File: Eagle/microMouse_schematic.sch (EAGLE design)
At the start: 50 parts, among them IC1 DSPIC33FJ64MC804-PT, IC2 L293D, IC3 LM7805, IC4 LM7833, X1 22-23-2021

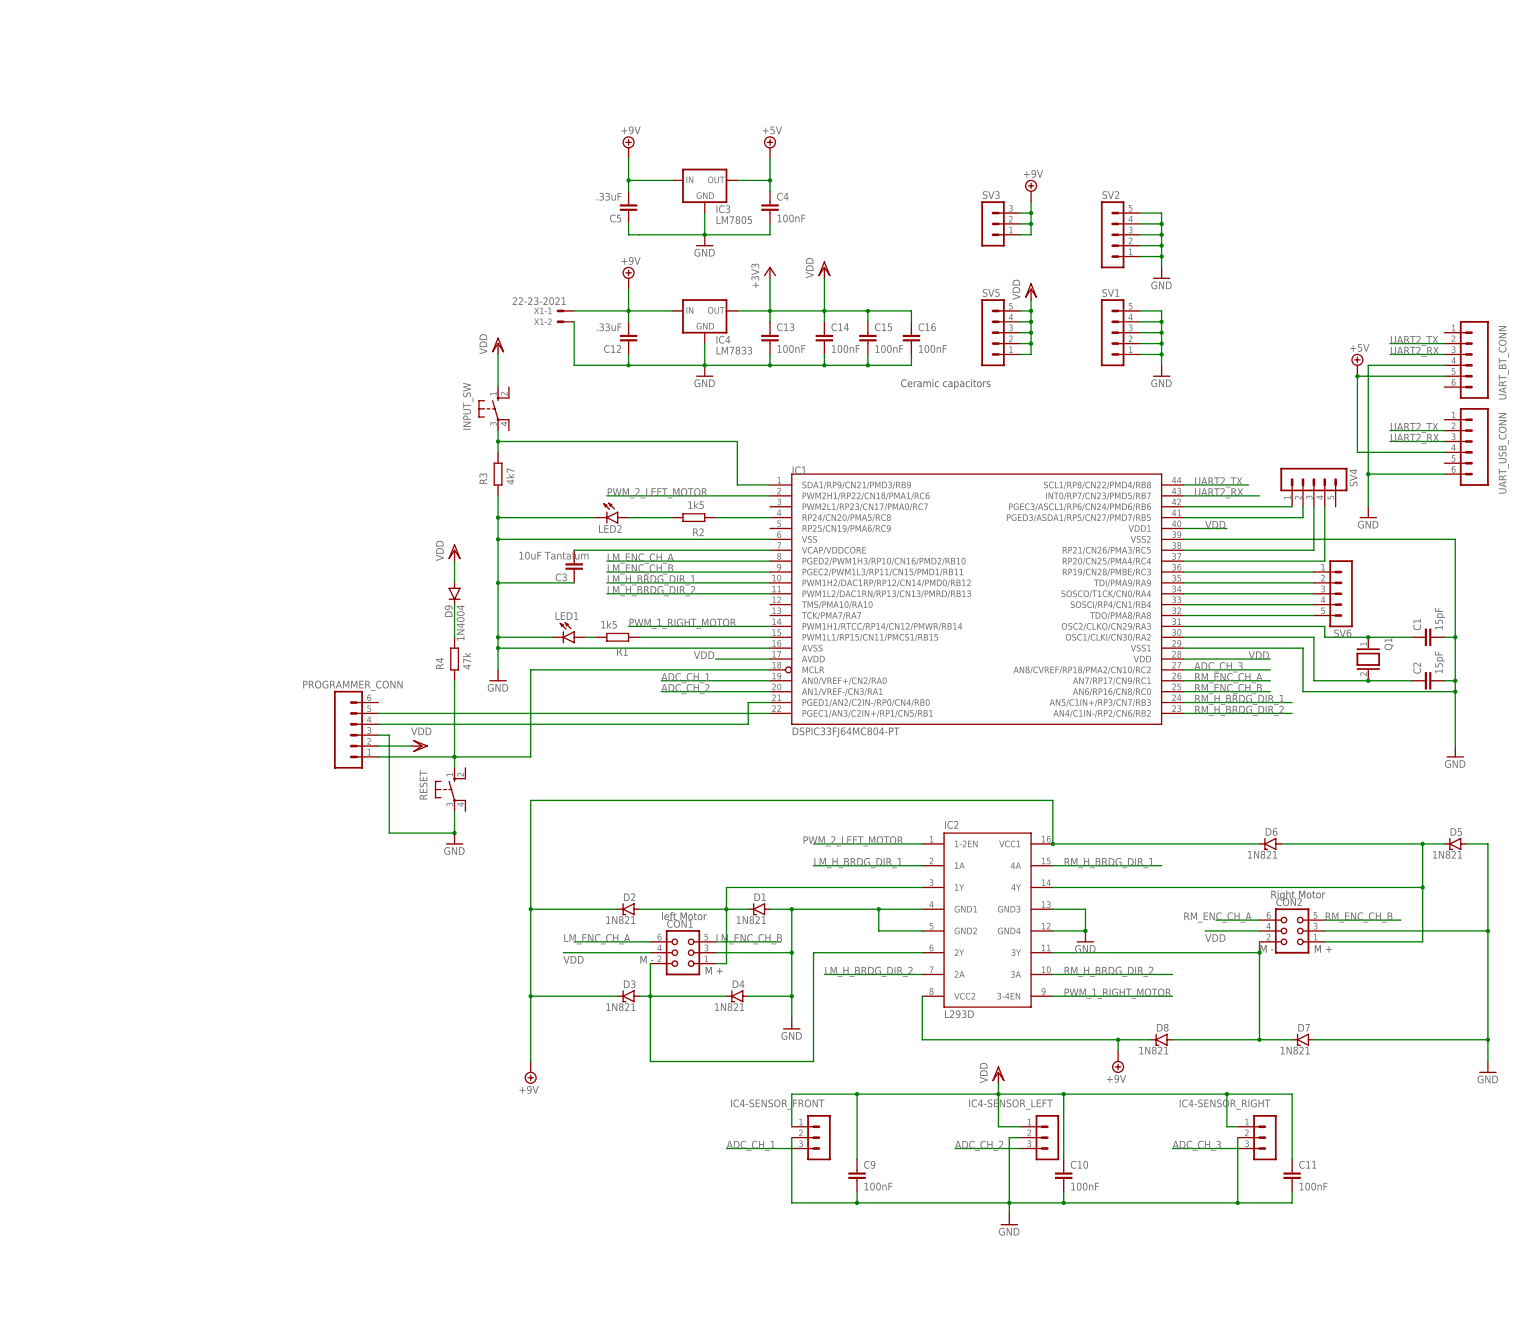
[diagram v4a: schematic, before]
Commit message: update schematic, finish placing components on board
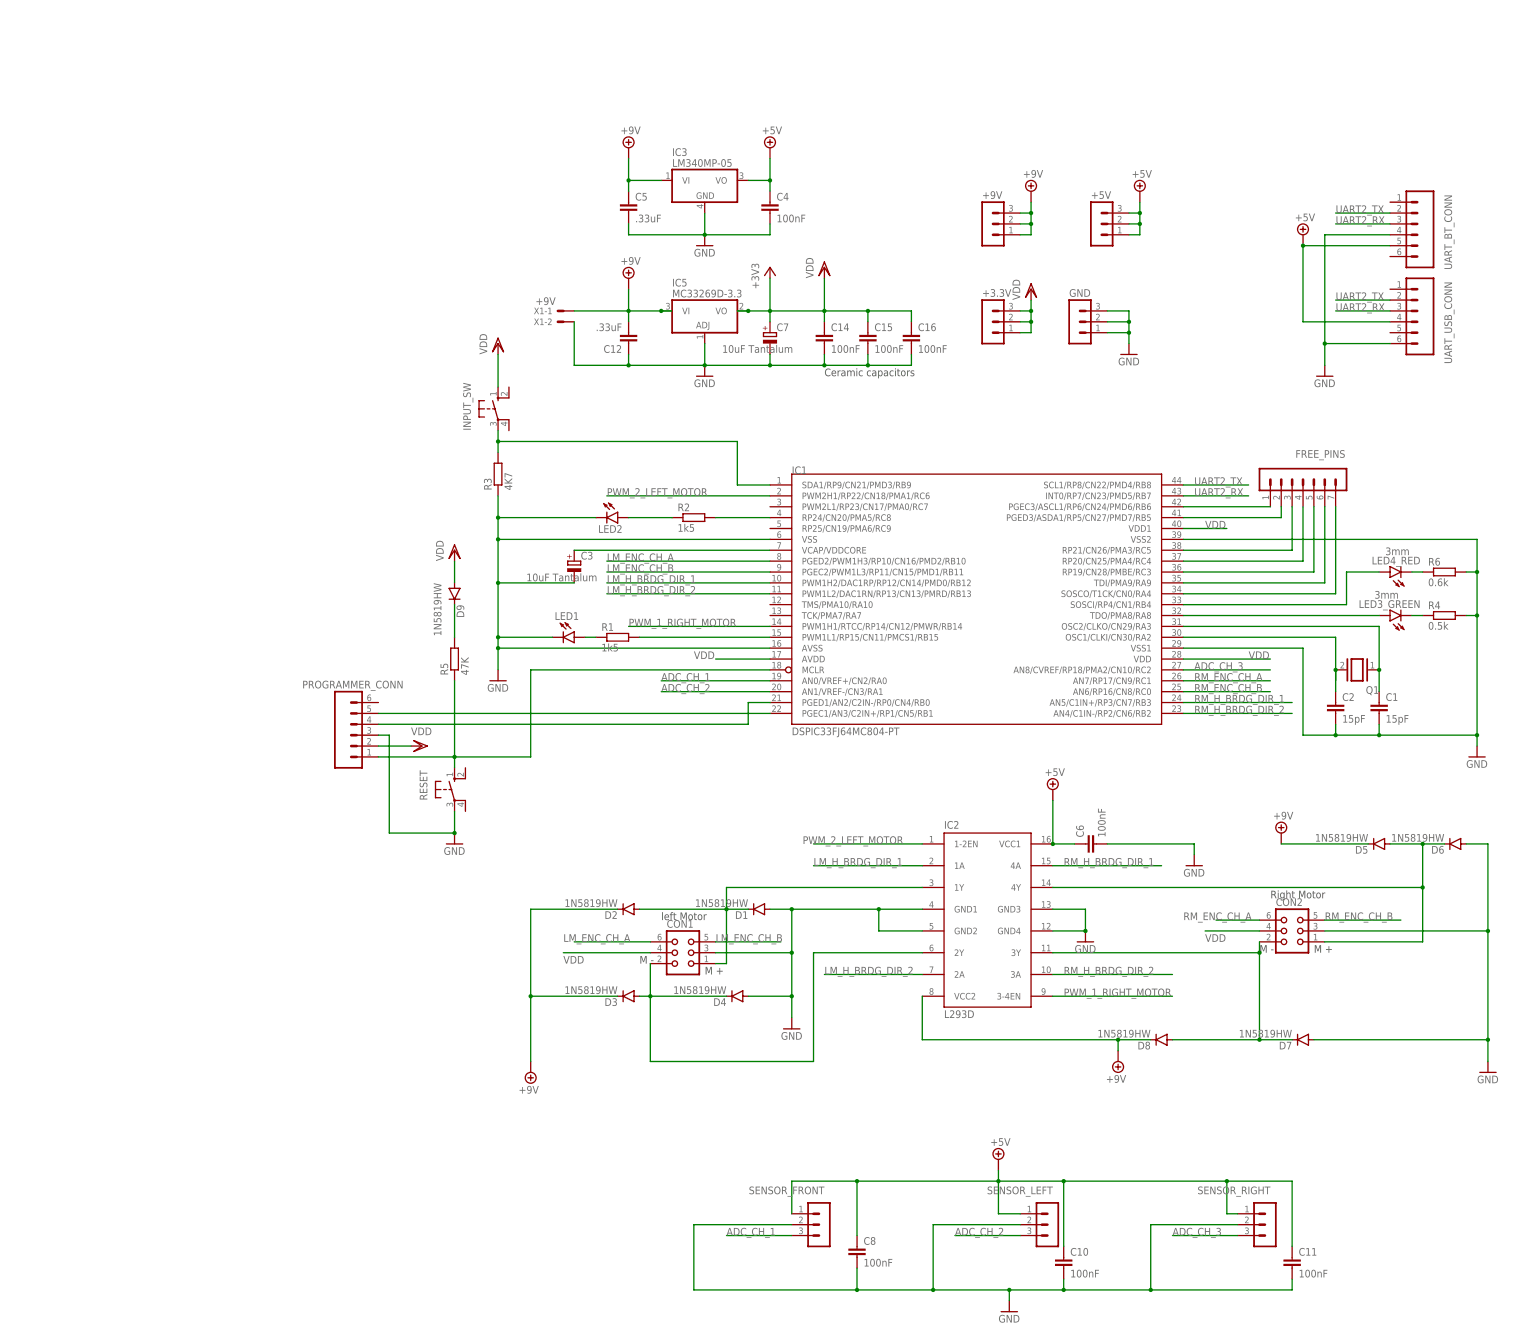
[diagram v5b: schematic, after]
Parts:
- removed C13, C9: 100nF, capacitor-wima:C2,5-3
- removed IC4: LM7833, v-reg:78XXS
- removed IC4-SENSOR_FRONT, IC4-SENSOR_LEFT, IC4-SENSOR_RIGHT: (no value), con-lstb:MA03-1
- removed SV1, SV2, SV4, SV5, SV6: (no value), con-lstb:MA05-1
- added +3.3V, +5V, GND, SENSOR_FRONT, SENSOR_LEFT, SENSOR_RIGHT: (no value), con-lstb:MA03-1
- added C6, C8: 100nF, rcl:C-EUC0805
- added C7: 10uF Tantalum, rcl:CPOL-EUCT3216
- added FREE_PINS: (no value), con-lstb:MA07-1
- added IC5: MC33269D-3.3, linear:MC33269D-3.3
- added LED3_GREEN, LED4_RED: 3mm, led:LEDB155
- added R5: 47K, rcl:R-EU_R0805
- added R6: 0.6k, rcl:R-EU_R0805
- C1, C10, C11, C12, C14, C15, C16, C2, C4, C5: device capacitor-wima:C2,5-3 -> rcl:C-EUC0805
- C3: device capacitor-wima:C2,5-3 -> rcl:CPOL-EUCT3216
- D1, D2, D3, D4, D5, D6, D7, D8: value 1N821 -> 1N5819HW; device diode:1N821 -> diode:CGRM4001-G
- D9: value 1N4004 -> 1N5819HW; device diode:1N4004 -> diode:CGRM4001-G
- IC3: value LM7805 -> LM340MP-05; device v-reg:78XXS -> linear:LM340MP-05
- R1, R2: device ngspice-simulation:R -> rcl:R-EU_R0805
- R3: value 4k7 -> 4K7; device ngspice-simulation:R -> rcl:R-EU_R0805
- R4: value 47k -> 0.5k; device ngspice-simulation:R -> rcl:R-EU_R0805
- X1: value 22-23-2021 -> +9V
- renumbered SV3 to +9V
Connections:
- new net N$13: LED3_GREEN.C, R4.1
- new net N$25: LED4_RED.C, R6.1
- net +5V: now also +5V.1, +5V.2, +5V.3, C10.1, C11.1, C6.1, C8.1, IC2.VCC1, IC3.VO, SENSOR_FRONT.1, SENSOR_LEFT.1, SENSOR_RIGHT.1; no longer IC3.OUT
- net +9V: now also C5.1, D5.C, IC3.VI, IC5.VI; no longer C5.2, D6.C, IC2.VCC1, IC3.IN, IC4.IN
- net ADC_CH_1: now also SENSOR_FRONT.3; no longer IC4-SENSOR_FRONT.3
- net ADC_CH_2: now also SENSOR_LEFT.3; no longer IC4-SENSOR_LEFT.3
- net ADC_CH_3: now also SENSOR_RIGHT.3; no longer IC4-SENSOR_RIGHT.3
- net GND: now also C3.-, C5.2, C6.2, C7.-, C8.2, D6.A, GND.1, GND.2, GND.3, IC5.ADJ, R4.2, R6.2, SENSOR_FRONT.2, SENSOR_LEFT.2, SENSOR_RIGHT.2; no longer C13.2, C3.1, C5.1, C9.2, D5.A, IC4-SENSOR_FRONT.2, IC4-SENSOR_LEFT.2, IC4-SENSOR_RIGHT.2, IC4.GND, SV1.1, SV1.2, SV1.3, SV1.4, SV1.5, SV2.1, SV2.2, SV2.3, SV2.4, SV2.5
- net N$1: now also R2.2; no longer R2.1
- net N$14: now also R1.2; no longer R1.1
- net N$15: now also LED4_RED.A; no longer SV6.4
- net N$16: now also FREE_PINS.7; no longer SV6.3
- net N$17: now also R1.1; no longer R1.2
- net N$18: now also FREE_PINS.6; no longer SV6.2
- net N$19: now also R5.2; no longer R4.2
- net N$2: now also D5.A, D6.C; no longer D5.C, D6.A
- net N$20: now also FREE_PINS.5; no longer SV6.1
- net N$21: now also FREE_PINS.4; no longer SV4.4
- net N$22: now also FREE_PINS.1; no longer SV4.1
- net N$23: now also FREE_PINS.2; no longer SV4.2
- net N$24: now also FREE_PINS.3; no longer SV4.3
- net N$3: now also R2.1; no longer R2.2
- net N$9: now also LED3_GREEN.A; no longer SV6.5
- net RESET: now also R5.1; no longer R4.1
- net VCAP/VDDCORE: now also C3.+; no longer C3.2
- net VDD: now also +3.3V.1, +3.3V.2, +3.3V.3, C7.+, IC5.VO; no longer C10.1, C11.1, C13.1, C9.1, IC4-SENSOR_FRONT.1, IC4-SENSOR_LEFT.1, IC4-SENSOR_RIGHT.1, IC4.OUT, SV5.1, SV5.2, SV5.3, SV5.4, SV5.5
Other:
- moved on the sheet: C1, C10, C11, C2, C5, Q1, R1, R2, R4, UART_BT_CONN, UART_USB_CONN

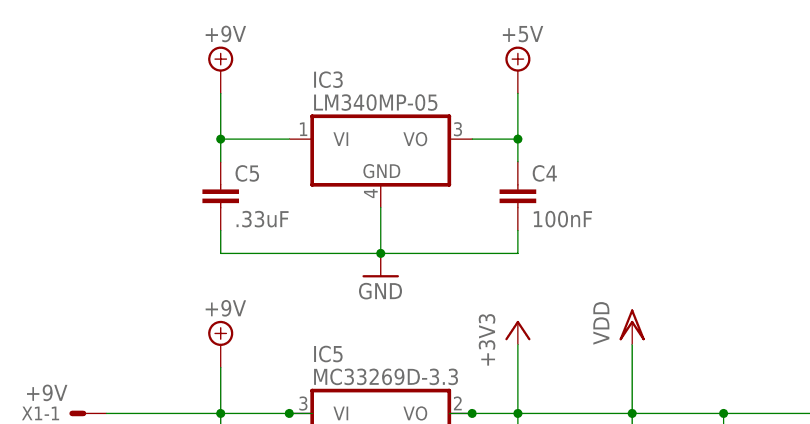
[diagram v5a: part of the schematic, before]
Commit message: PCB signals routing
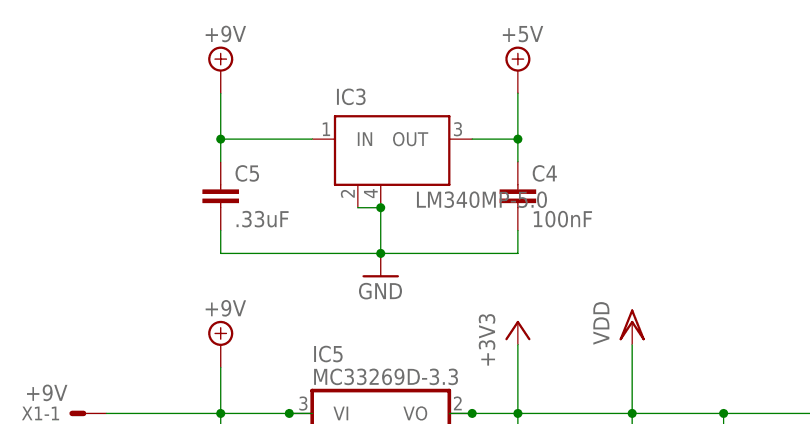
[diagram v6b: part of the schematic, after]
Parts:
- IC3: value LM340MP-05 -> LM340MP-5.0; device linear:LM340MP-05 -> linear:LM340S
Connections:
- net +5V: now also IC3.OUT; no longer IC3.VO
- net +9V: now also IC3.IN; no longer IC3.VI
- net GND: now also IC3.GND@1, IC3.GND@2; no longer IC3.GND
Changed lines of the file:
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@@
 <part name="C7" library="rcl" library_urn="urn:adsk.eagle:library:334" deviceset="CPOL-EU" device="CT3216" package3d_urn="urn:adsk.eagle:package:23327/2" value="10uF Tantalum"/>
 <part name="R3" library="rcl" library_urn="urn:adsk.eagle:library:334" deviceset="R-EU_" device="R0805" package3d_urn="urn:adsk.eagle:package:23553/2" value="4K7"/>
-<part name="IC3" library="linear" library_urn="urn:adsk.eagle:library:262" deviceset="LM340?-*" device="MP" package3d_urn="urn:adsk.eagle:package:28541/2" technology="05"/>
 <part name="GND" library="con-lstb" library_urn="urn:adsk.eagle:library:162" deviceset="MA03-1" device="" package3d_urn="urn:adsk.eagle:package:8339/1"/>
 <part name="+3.3V" library="con-lstb" library_urn="urn:adsk.eagle:library:162" deviceset="MA03-1" device="" package3d_urn="urn:adsk.eagle:package:8339/1"/>
@@
 <part name="R4" library="rcl" library_urn="urn:adsk.eagle:library:334" deviceset="R-EU_" device="R0805" package3d_urn="urn:adsk.eagle:package:23553/2" value="0.5k"/>
 <part name="R6" library="rcl" library_urn="urn:adsk.eagle:library:334" deviceset="R-EU_" device="R0805" package3d_urn="urn:adsk.eagle:package:23553/2" value="0.6k"/>
+<part name="IC3" library="linear" library_urn="urn:adsk.eagle:library:262" deviceset="LM340S" device="" package3d_urn="urn:adsk.eagle:package:28541/2" value="LM340MP-5.0"/>
 </parts>
 <sheets>
@@
 <attribute name="VALUE" x="-187.198" y="158.75" size="1.778" layer="96" rot="R90"/>
 </instance>
-<instance part="IC3" gate="A" x="-142.24" y="231.14" smashed="yes">
-<attribute name="NAME" x="-149.86" y="236.855" size="1.778" layer="95"/>
-<attribute name="VALUE" x="-149.86" y="234.315" size="1.778" layer="96"/>
-</instance>
 <instance part="GND" gate="G$1" x="-55.88" y="198.12" smashed="yes">
 <attribute name="VALUE" x="-57.15" y="190.5" size="1.778" layer="96"/>
@@
 <attribute name="NAME" x="26.67" y="141.1986" size="1.778" layer="95"/>
 <attribute name="VALUE" x="26.67" y="136.398" size="1.778" layer="96"/>
+</instance>
+<instance part="IC3" gate="G$1" x="-142.24" y="228.6" smashed="yes">
+<attribute name="NAME" x="-147.32" y="234.95" size="1.778" layer="95"/>
+<attribute name="VALUE" x="-138.43" y="223.52" size="1.778" layer="96"/>
 </instance>
 </instances>
@@
 <wire x1="-127" y1="218.44" x2="-127" y2="220.98" width="0.1524" layer="91"/>
 <wire x1="-160.02" y1="220.98" x2="-160.02" y2="218.44" width="0.1524" layer="91"/>
-<pinref part="IC3" gate="A" pin="GND"/>
 <pinref part="C5" gate="G$1" pin="2"/>
+<pinref part="IC3" gate="G$1" pin="GND@2"/>
+<pinref part="IC3" gate="G$1" pin="GND@1"/>
+<wire x1="-144.78" y1="223.52" x2="-142.24" y2="223.52" width="0.1524" layer="91"/>
+<junction x="-142.24" y="223.52"/>
 </segment>
 <segment>
@@
 <pinref part="SUPPLY3" gate="G$1" pin="+9V"/>
 <wire x1="-160.02" y1="228.6" x2="-160.02" y2="231.14" width="0.1524" layer="91"/>
-<pinref part="IC3" gate="A" pin="VI"/>
 <wire x1="-160.02" y1="231.14" x2="-160.02" y2="236.22" width="0.1524" layer="91"/>
-<wire x1="-152.4" y1="231.14" x2="-160.02" y2="231.14" width="0.1524" layer="91"/>
+<wire x1="-149.86" y1="231.14" x2="-160.02" y2="231.14" width="0.1524" layer="91"/>
 <junction x="-160.02" y="231.14"/>
 <pinref part="C5" gate="G$1" pin="1"/>
+<pinref part="IC3" gate="G$1" pin="IN"/>
 </segment>
 <segment>
@@
 <pinref part="C4" gate="G$1" pin="1"/>
 <pinref part="SUPPLY5" gate="+5V" pin="+5V"/>
-<pinref part="IC3" gate="A" pin="VO"/>
 <wire x1="-127" y1="231.14" x2="-127" y2="228.6" width="0.1524" layer="91"/>
 <wire x1="-132.08" y1="231.14" x2="-127" y2="231.14" width="0.1524" layer="91"/>
 <junction x="-127" y="231.14"/>
-</segment>
-<segment>
+<pinref part="IC3" gate="G$1" pin="OUT"/>
+</segment>
+<segment>

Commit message: add motor & sensor mounts, add GND planes
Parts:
- removed IC5: MC33269D-3.3, linear:MC33269D-3.3
- added BUZZER: (no value), con-lstb:MA03-1
- added IC4: LM3940IMP-3.3, linear:LM340S
- added RGB_LED: (no value), con-lstb:MA04-1
- added SENS_MNT_F: SENSOR_MOUNT_F, linear:SENSOR_MOUNT
- added SENS_MNT_L: SENSOR_MOUNT_L, linear:SENSOR_MOUNT
- added SENS_MNT_R: SENSOR_MOUNT_R, linear:SENSOR_MOUNT
- added U$1, U$2: MOTOR_MOUNT, linear:MOTOR_MOUNT
- C7: value 10uF Tantalum -> 33uF Tantalum; device rcl:CPOL-EUCT3216 -> rcl:CPOL-EUCT7343
- FREE_PINS: device con-lstb:MA07-1 -> con-lstb:MA03-1
- renumbered X1 to 9V-INPUT
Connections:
- net +5V: now also BUZZER.1
- net +9V: now also IC4.IN; no longer IC5.VI
- net GND: now also BUZZER.3, IC4.GND@1, IC4.GND@2, RGB_LED.1, SENS_MNT_F.P$1, SENS_MNT_F.P$2, SENS_MNT_L.P$1, SENS_MNT_L.P$2, SENS_MNT_R.P$1, SENS_MNT_R.P$2, U$1.P$1, U$1.P$2, U$2.P$1, U$2.P$2; no longer IC5.ADJ
- net N$16: now also RGB_LED.4; no longer FREE_PINS.7
- net N$18: now also RGB_LED.3; no longer FREE_PINS.6
- net N$20: now also RGB_LED.2; no longer FREE_PINS.5
- net N$21: now also BUZZER.2; no longer FREE_PINS.4
- net VDD: now also IC4.OUT; no longer IC5.VO
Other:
- note added: "Motors & Sensors Mounts"
